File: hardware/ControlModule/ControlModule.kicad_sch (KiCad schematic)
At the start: 0 parts

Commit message: AS OF 20/1/2024
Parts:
- added C1: 100nF, Capacitor_SMD:C_1206_3216Metric_Pad1.33x1.80mm_HandSolder, symbol Device:C
- added C2: 1uF, Capacitor_SMD:C_1206_3216Metric_Pad1.33x1.80mm_HandSolder, symbol Device:C
- added D1: WS2812B-2020, esp-map-footprints:LED_WS2812-2020, symbol LED:WS2812B
- added FID1, FID2, FID3: Fiducial, Fiducial:Fiducial_0.5mm_Mask1mm, symbol Mechanical:Fiducial
- added H1, H2: MountingHole_Pad, MountingHole:MountingHole_3.5mm_Pad, symbol Mechanical:MountingHole_Pad
- added J1: ICSP, Connector_PinSocket_2.54mm:PinSocket_1x06_P2.54mm_Vertical, symbol Connector_Generic:Conn_01x06
- added J10, J11, J5, J6, J8, J9: Conn_01x02, esp-map-footprints:TerminalBlock-Bornier-2_P5.08mm, symbol Connector_Generic:Conn_01x02
- added J2: Conn_01x03, Connector_Molex:Molex_KK-254_AE-6410-03A_1x03_P2.54mm_Vertical, symbol Connector_Generic:Conn_01x03
- added J3: I2C/ICSP/UART, Connector_PinSocket_2.54mm:PinSocket_2x07_P2.54mm_Vertical, symbol Connector_Generic:Conn_02x07_Odd_Even
- added J4: Conn_01x06, Connector_Molex:Molex_KK-254_AE-6410-06A_1x06_P2.54mm_Vertical, symbol Connector_Generic:Conn_01x06
- added J7: ICSP, Connector_PinHeader_2.54mm:PinHeader_2x03_P2.54mm_Vertical, symbol Connector_Generic:Conn_02x03_Odd_Even
- added Q1: BC817, Package_TO_SOT_SMD:SOT-23, symbol Transistor_BJT:BC817
- added Q2: IRLML2502, Package_TO_SOT_SMD:SOT-23, symbol Transistor_FET:IRLML0030
- added R1: 1k, Resistor_SMD:R_1206_3216Metric, symbol Device:R
- added R10, R11, R12: ?, Resistor_THT:R_Axial_DIN0207_L6.3mm_D2.5mm_P2.54mm_Vertical, symbol Device:R
- added R13, R15, R16, R2, R3, R8, R9: 10k, Resistor_SMD:R_1206_3216Metric, symbol Device:R
- added R14: 100, Resistor_SMD:R_1206_3216Metric, symbol Device:R
- added R4, R5, R6, R7: 100k, Resistor_SMD:R_1206_3216Metric, symbol Device:R
- added U1: lan8720_eth_board, esp-map-footprints:LAN8720-ETH-BOARD-90deg-CON-BOT, symbol esp-map-devices:LAN8720_Eth_Board
- added U2: DS1233A-10, Package_TO_SOT_THT:TO-92, symbol esp-map-devices:DS1233
- added U3: PC847, Package_DIP:SMDIP-16_W9.53mm, symbol Isolator:PC847
- added U4: ESP32-WROOM-32, RF_Module:ESP32-WROOM-32, symbol RF_Module:ESP32-WROOM-32
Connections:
- new net: R10.1, U3.1
- new net: J8.2 (Pin_2), U3.2
- new net: Q1.1 (B), R1.1
- new net: Q1.3 (C), Q2.1 (G), R2.2
- new net: J10.1 (Pin_1), R12.2
- new net: J10.2 (Pin_2), U3.6
- new net: J2.3 (Pin_3), Q2.3 (D)
- new net: J8.1 (Pin_1), R10.2
- new net: R14.2, U3.7
- new net: R11.1, U3.3
- new net: J9.2 (Pin_2), U3.4
- new net: R12.1, U3.5
- new net: J11.1 (Pin_1), U3.10
- new net: J11.2 (Pin_2), U3.9
- new net: J9.1 (Pin_1), R11.2
- new net +12V: J2.1 (Pin_1), J6.1 (Pin_1), R2.1
- new net +3.3V: U4.2 (VDD)
- new net +3V3: C1.1, C2.1, J1.6 (Pin_6), J3.10 (Pin_10), J3.11 (Pin_11), J3.12 (Pin_12), J4.4 (Pin_4), J5.1 (Pin_1), J7.2 (Pin_2), R13.1, R15.1, R16.1, R3.1, R4.2, R5.2, R6.1, R7.1, R8.1, U1.13 (VCC), U1.14 (VCC), U2.3 (VDD)
- new net +5V: D1.1 (VDD), J3.1 (Pin_1), J3.2 (Pin_2), J4.5 (Pin_5), J5.2 (Pin_2)
- new net CRS: U1.8 (CRS), U4.12 (IO27)
- new net GND: C1.2, C2.2, D1.3 (VSS), H1.1, H2.1, J1.5 (Pin_5), J3.13 (Pin_13), J3.14 (Pin_14), J4.6 (Pin_6), J6.2 (Pin_2), J7.3 (Pin_3), Q1.2 (E), Q2.2 (S), R9.1, U1.11 (GND), U1.12 (GND), U2.1 (GND), U3.11, U3.13, U3.15, U3.8, U4.1 (GND), U4.15 (GND), U4.38 (GND), U4.39 (GND)
- new net GPIO0: J1.4 (Pin_4), R8.2, U1.7 (nRST/REFCLK), U4.25 (IO0)
- new net I0: R13.2, U3.16, U4.7 (IO35)
- new net I1: R15.2, U3.14, U4.4 (SENSOR_VP)
- new net I2: R16.2, U3.12, U4.5 (SENSOR_VN)
- new net INT: J3.4 (Pin_4), J4.1 (Pin_1), U4.6 (IO34)
- new net MCLR: J3.5 (Pin_5), J7.1 (Pin_1)
- new net MDC: U1.10 (MDC), U4.37 (IO23)
- new net MDIO: U1.9 (MDIO), U4.30 (IO18)
- new net OSC_E: R9.2, U1.2 (OSC_E), U4.28 (IO17)
- new net P0: R1.2, U4.14 (IO12)
- new net PGC: J3.9 (Pin_9), J7.5 (Pin_5)
- new net PGD: J3.7 (Pin_7), J7.4 (Pin_4)
- new net RA5: J3.3 (Pin_3), J7.6 (Pin_6)
- new net RESET: J1.1 (Pin_1), R3.2, U2.2 (~{RESET}), U4.3 (EN)
- new net RGBLED: D1.4 (DIN), U4.24 (IO2)
- new net RX0: U1.5 (RX0), U4.10 (IO25)
- new net RX1: U1.6 (RX1), U4.11 (IO26)
- new net RXD0: J1.3 (Pin_3), U4.34 (RXD0/IO3)
- new net S0: R14.1, U4.26 (IO4)
- new net SCL: J3.6 (Pin_6), J4.2 (Pin_2), R4.1, R7.2, U4.8 (IO32)
- new net SDA: J3.8 (Pin_8), J4.3 (Pin_3), R5.1, R6.2, U4.9 (IO33)
- new net TX0: U1.4 (TX0), U4.31 (IO19)
- new net TX1: U1.1 (TX1), U4.36 (IO22)
- new net TXD0: J1.2 (Pin_2), U4.35 (TXD0/IO1)
- new net TX_EN: U1.3 (TX_EN), U4.33 (IO21)
- no-connect marks 0 -> 8
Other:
- note added: "ETHERNET MODULE"
- note added: "I2C HEADER"
- note added: "ICSP HEADER"
- note added: "INTER-PCB Connector"
- note added: "MCU"
- note added: "MNT. Holes & FIDUCIALS"
- note added: "ONBOARD LED"
- note added: "OPTO I/O"
- note added: "PGD -> RX PGC -> TX (for pic)"
- note added: "POWER MONITOR"
- note added: "POWER OUT"
- note added: "POWER OUTPUT"
- note added: "UART2 (UPSM.Module)"
- note added: "https://sautter.com/blog/ethernet-on-esp32-using-lan8720/"

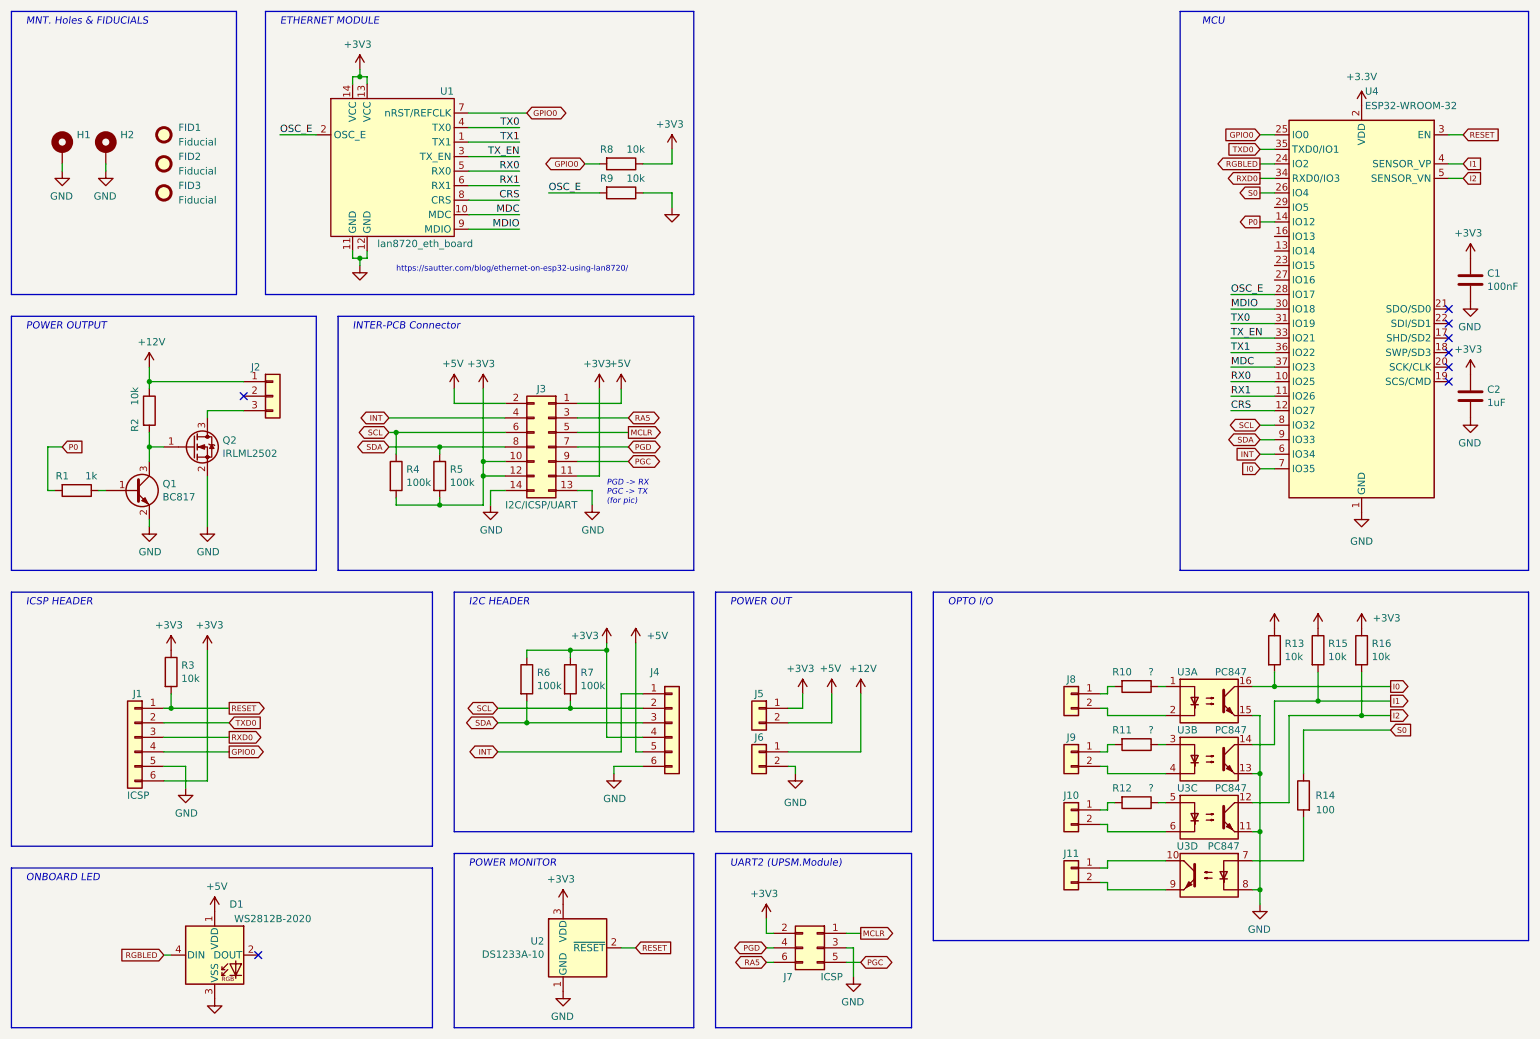
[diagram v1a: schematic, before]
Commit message: add some new PCB's
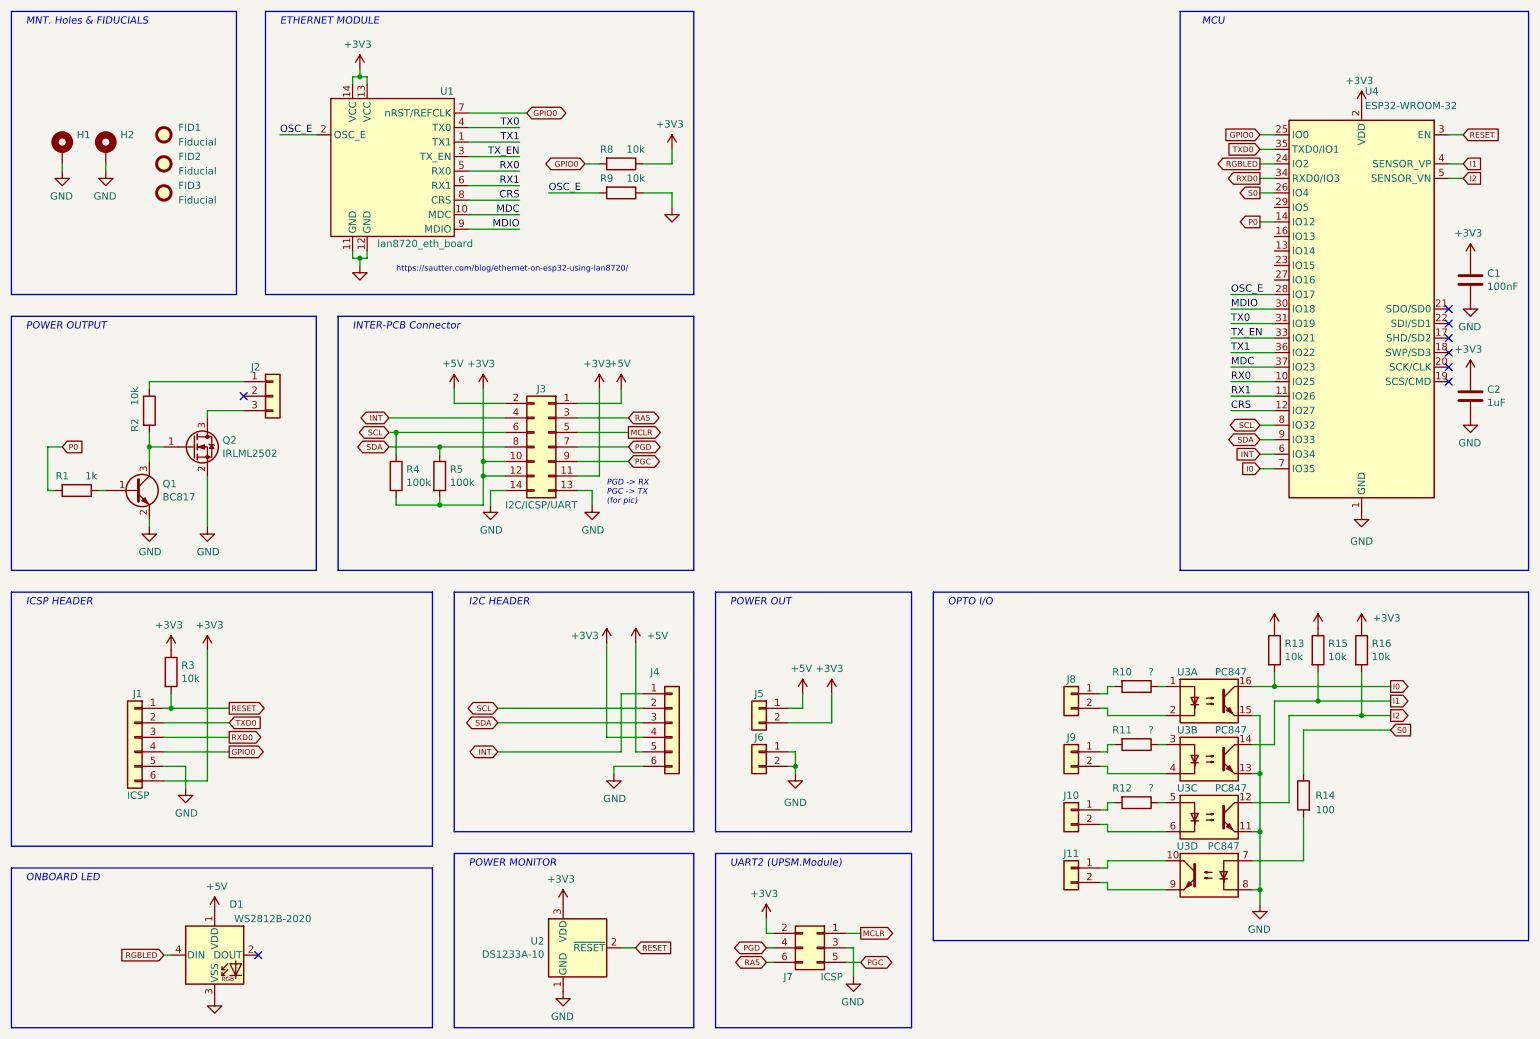
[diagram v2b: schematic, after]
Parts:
- removed R6, R7: 100k, Resistor_SMD:R_1206_3216Metric, symbol Device:R
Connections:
- net +3.3V is gone; now on net +3V3: U4.2 (VDD)
- net +3V3: now also J5.2 (Pin_2); no longer J5.1 (Pin_1)
- net +5V: now also J5.1 (Pin_1); no longer J5.2 (Pin_2)
- net GND: now also J6.1 (Pin_1)
- net +12V: no longer names the net of J2.1 (Pin_1), R2.1
- net +12V: no longer J6.1 (Pin_1)
